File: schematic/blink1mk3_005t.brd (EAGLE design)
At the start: 15.7 x 13.7 mm, 14 parts, among them U1 EFM32HG309F64G, X1 USB

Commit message: fix EFM32HG309 pad spacing issue. omg what a slog
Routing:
- net CAP0A: track 12.9 -> 14.2 mm
- net +5V: track 32.9 -> 32.0 mm

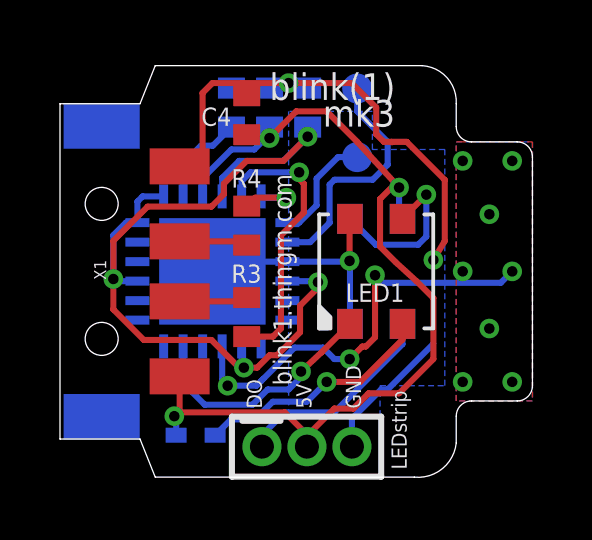
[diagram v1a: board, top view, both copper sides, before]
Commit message: fix QFN footprint again, add blink1mk3_card2
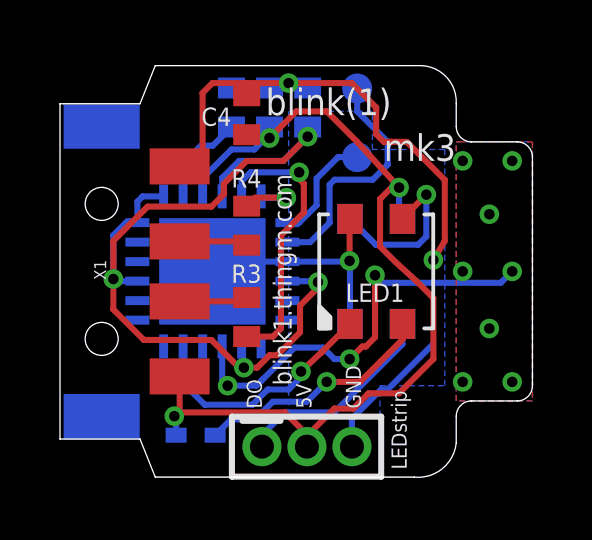
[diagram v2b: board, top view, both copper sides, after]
